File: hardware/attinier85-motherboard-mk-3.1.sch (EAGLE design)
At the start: 14 parts, among them IC1 Tiny85, IC2 LM2931, U1 ATTINIEST85_SHIELDV2

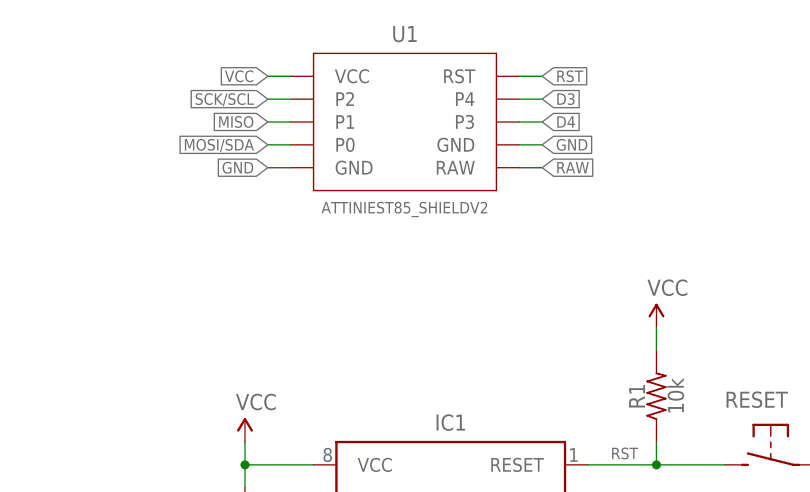
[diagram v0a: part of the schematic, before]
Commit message: renaming parts
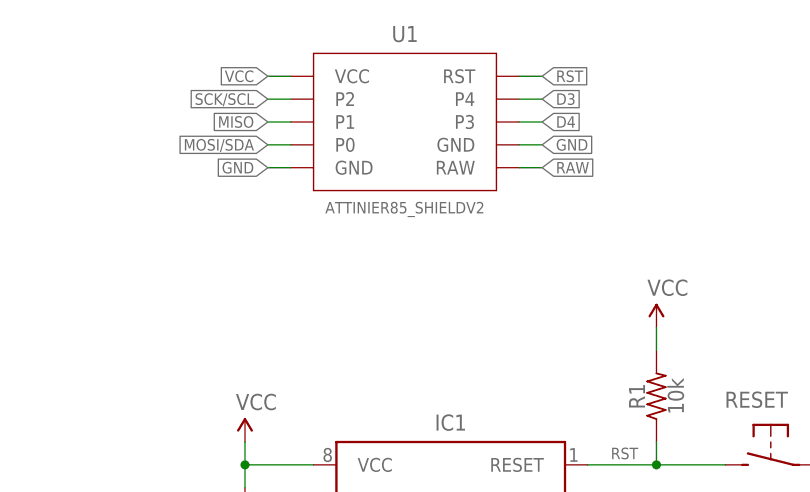
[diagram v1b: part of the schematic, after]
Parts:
- U1: value ATTINIEST85_SHIELDV2 -> ATTINIER85_SHIELDV2; device A_butts:ATTINIEST85_SHIELDV2 -> A_butts:ATTINIER85_SHIELDV2
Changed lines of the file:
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@@
 <part name="D1" library="A_butts" deviceset="DIODE" device="PTH-10.68MM" value="1N4001"/>
 <part name="TVS1" library="A_butts" deviceset="TVS" device="DO-41-TVS-BIDIRECTIONAL" value="12V"/>
-<part name="U1" library="A_butts" deviceset="ATTINIEST85_SHIELD" device="V2"/>
+<part name="U1" library="A_butts" deviceset="ATTINIER85_SHIELD" device="V2"/>
 </parts>
 <sheets>
